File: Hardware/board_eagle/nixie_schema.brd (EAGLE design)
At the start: 150 x 170 mm, 230 parts, among them P1 100k, P2 10k, Q1 BC856B, Q3 BC856B, Q4 BCX70H, Q5 NTF5P03, U2 MC7940N, U3 1V5

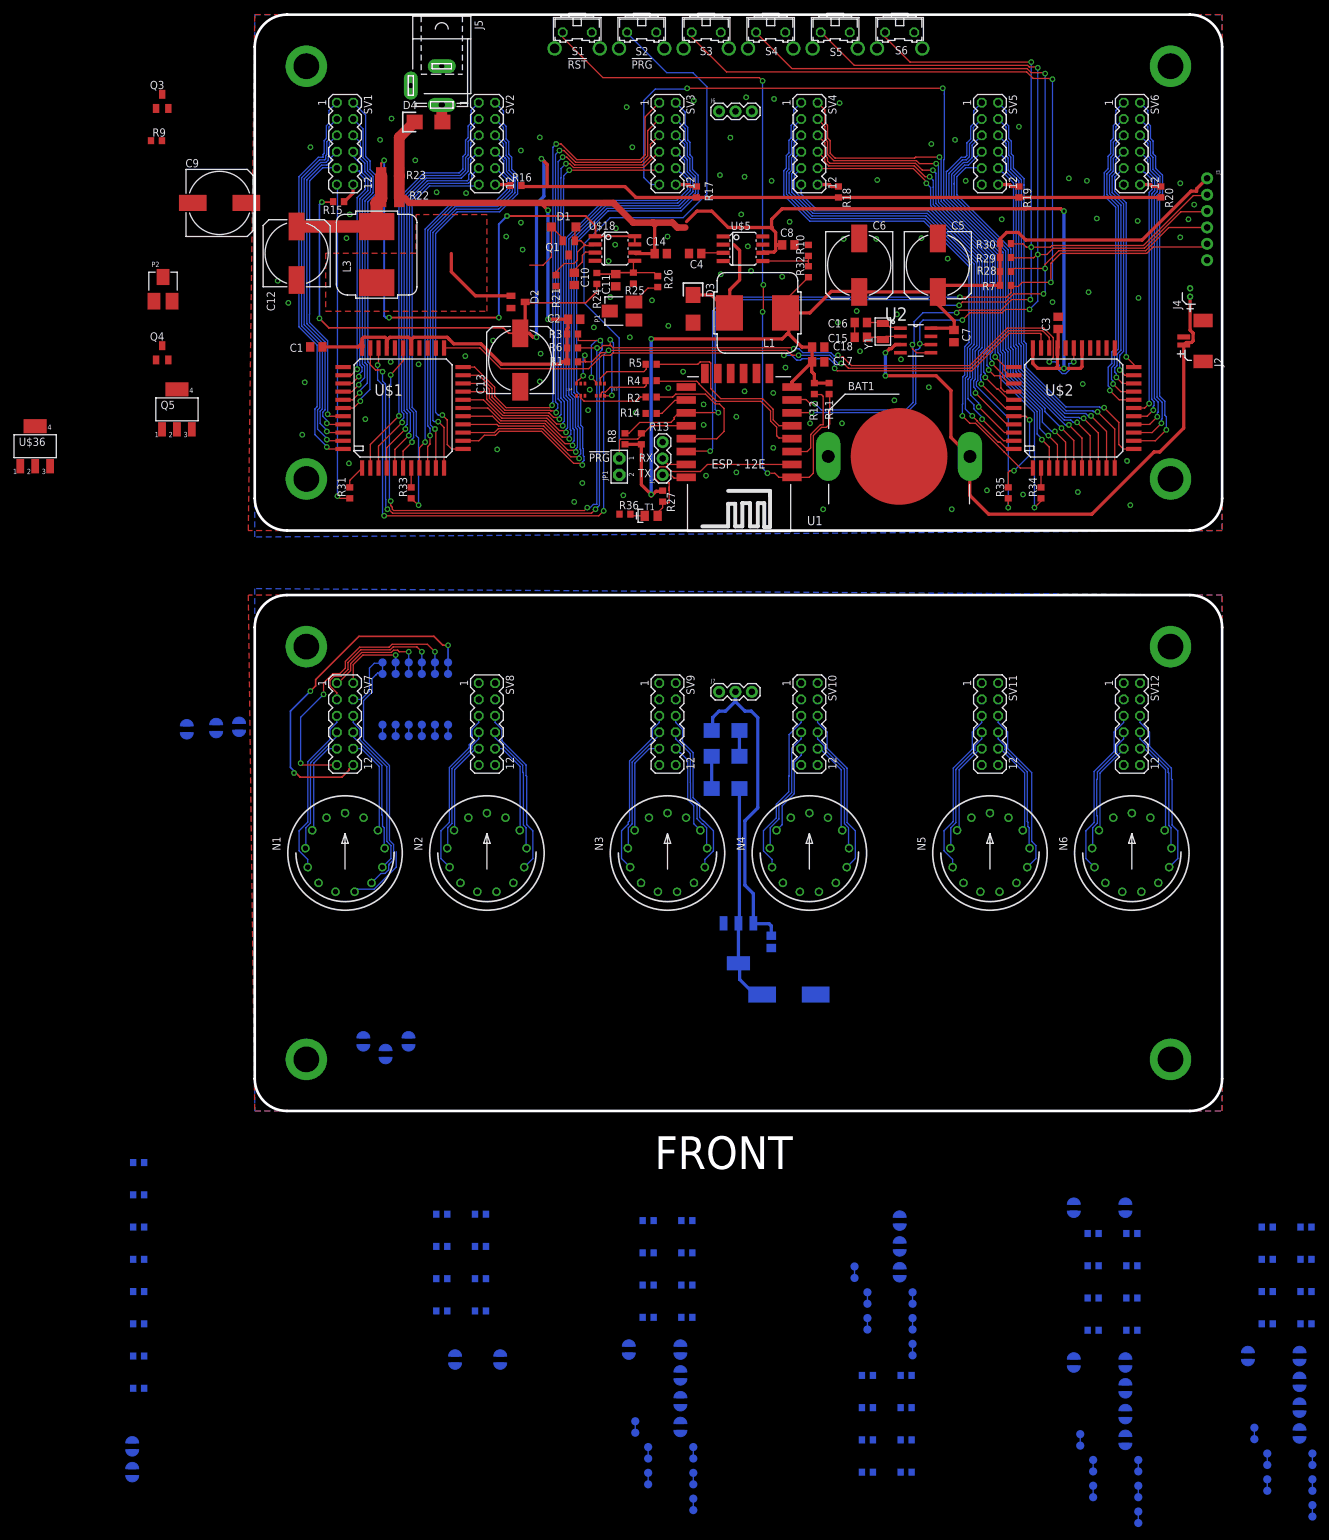
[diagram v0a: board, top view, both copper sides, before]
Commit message: Some more routing of the top board
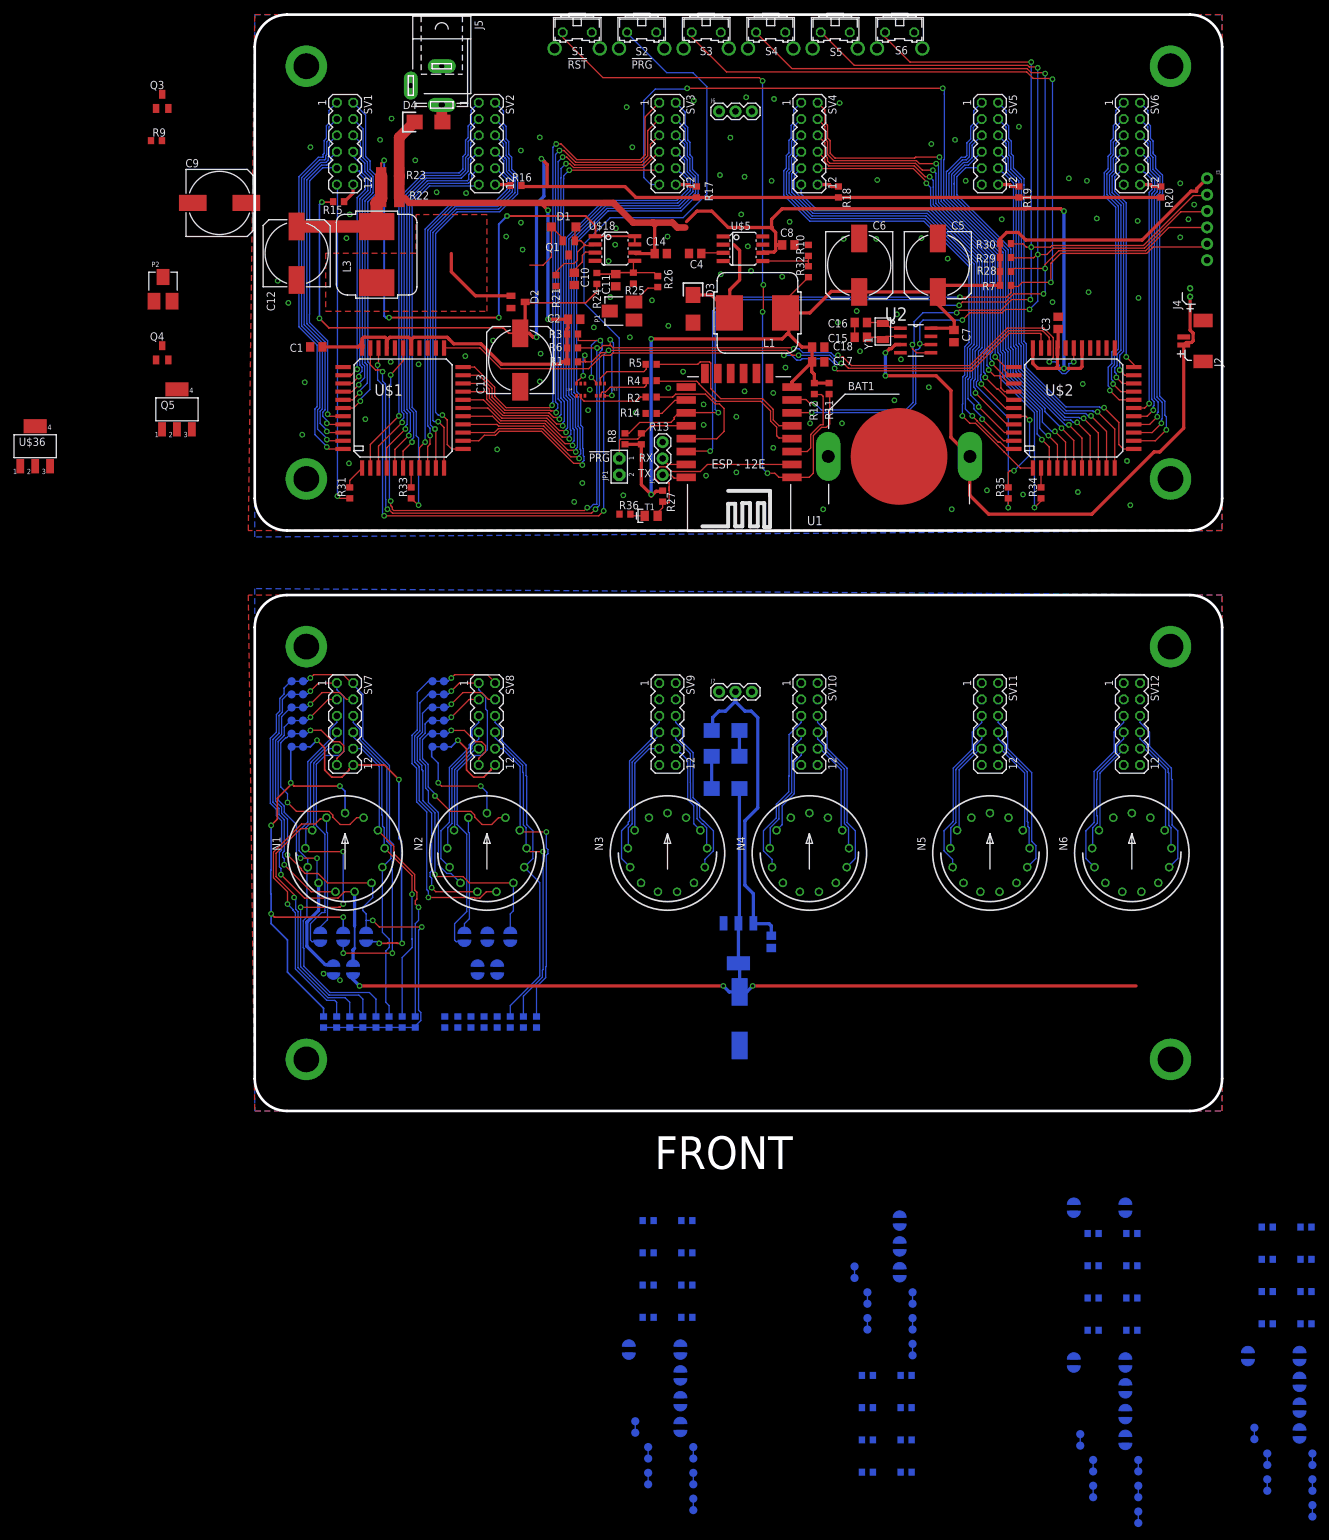
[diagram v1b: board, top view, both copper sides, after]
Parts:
- CUT1, CUT10, CUT11, CUT12, CUT13, CUT14, CUT15, CUT16, CUT17, CUT18, CUT19, CUT2, CUT20, CUT21, CUT22, CUT23, CUT24, CUT25, CUT26, CUT27, CUT28, CUT29, CUT3, CUT30, CUT31, CUT32, CUT33, CUT34, CUT35, CUT36, CUT4, CUT5, CUT6, CUT7, CUT8, CUT9: device nixe_cmp:CUT_TRACE -> nixe_cmp:CUT_TRACE_2
- moved BR2 85.1 mm to (15.2, -68.1), turned to 180 degrees
- moved BR7 80.2 mm to (12.2, -68.1)
- moved R44 65.6 mm to (14.7, -76.2), turned to 270 degrees
- moved R43 62.4 mm to (16.8, -76.2), turned to 270 degrees
- moved BR4 60.8 mm to (37.6, -68.1), turned to 180 degrees
- moved BR3 60.6 mm to (34.5, -68.1)
- moved R42 59.5 mm to (18.8, -76.2), turned to 270 degrees
- moved R41 57.1 mm to (20.8, -76.2), turned to 270 degrees
- moved R40 55.0 mm to (22.9, -76.2), turned to 270 degrees
- moved R39 53.4 mm to (24.9, -76.2), turned to 270 degrees
- moved R52 45.0 mm to (33.5, -76.2), turned to 270 degrees
- moved R51 44.8 mm to (35.6, -76.2), turned to 270 degrees
- moved BR1 42.5 mm to (17.3, -63.0)
- moved R38 40.8 mm to (12.7, -76.2), turned to 270 degrees
- moved R50 40.7 mm to (37.6, -76.2), turned to 270 degrees
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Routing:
- net 1V5: track 34.8 -> 155.6 mm, vias 0 -> 3
- net 1_A_A: track 0.00 -> 72.5 mm, vias 0 -> 5
- net 1_LDP_G: track 0.00 -> 58.9 mm, vias 0 -> 1
- net N$23: track 0.00 -> 52.2 mm, vias 0 -> 1
- net N$10: track 11.3 -> 62.6 mm, vias 1 -> 3
- net 1_7_GRID: track 38.0 -> 87.6 mm, vias 0 -> 3
- net 2_7_GRID: track 0.00 -> 48.8 mm, vias 0 -> 1
- net 2_6_CAT: track 0.00 -> 47.1 mm, vias 0 -> 1
- net 1_6_CAT: track 10.4 -> 57.0 mm, vias 0 -> 1
- net 1_4_CAT: track 0.00 -> 45.9 mm, vias 0 -> 2
- net 1_2_E: track 20.0 -> 64.7 mm, vias 0 -> 3
- net 2_5_NC: track 0.00 -> 40.0 mm, vias 0 -> 1
- net 1_1_F: track 15.0 -> 53.9 mm, vias 0 -> 1
- net 1_5_NC: track 0.00 -> 38.5 mm, vias 0 -> 1
- net N$29: track 15.8 -> 52.6 mm
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
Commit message: Top board routing
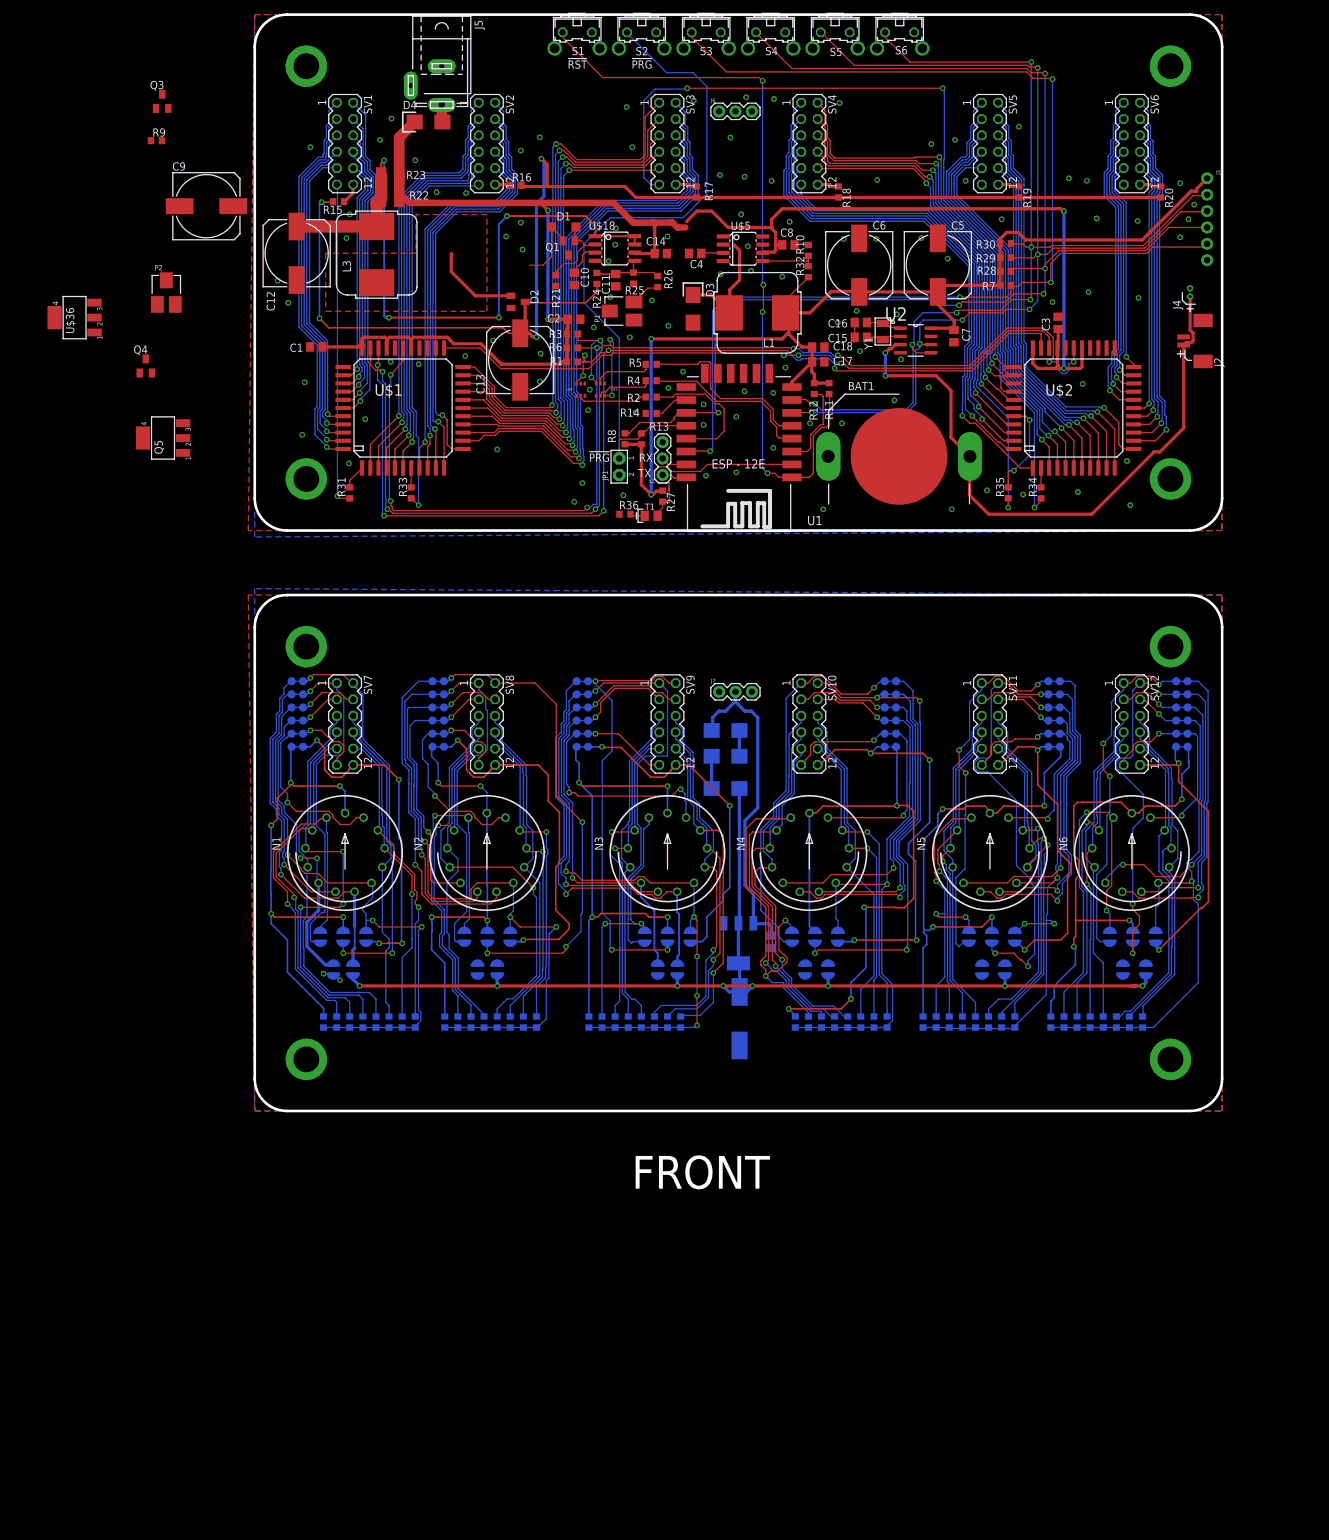
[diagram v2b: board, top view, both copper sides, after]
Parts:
- moved CUT30 130.3 mm to (124.0, -23.4), turned to 270 degrees
- moved CUT36 130.2 mm to (143.8, -23.4), turned to 270 degrees
- moved CUT18 126.8 mm to (50.8, -25.4), turned to 90 degrees
- moved CUT29 121.7 mm to (124.0, -27.4), turned to 270 degrees
- moved CUT35 121.3 mm to (143.8, -27.4), turned to 270 degrees
- moved CUT15 120.1 mm to (50.8, -23.4), turned to 270 degrees
- moved CUT27 119.8 mm to (124.0, -25.4), turned to 90 degrees
- moved CUT33 119.3 mm to (143.8, -25.4), turned to 90 degrees
- moved CUT34 118.2 mm to (143.8, -31.5), turned to 270 degrees
- moved CUT28 118.2 mm to (124.0, -31.5), turned to 270 degrees
- moved CUT17 118.0 mm to (50.8, -29.5), turned to 90 degrees
- moved CUT14 116.8 mm to (50.8, -27.4), turned to 270 degrees
- moved CUT16 116.8 mm to (50.8, -31.5), turned to 90 degrees
- moved CUT32 116.3 mm to (143.8, -29.5), turned to 90 degrees
- moved CUT26 116.3 mm to (124.0, -29.5), turned to 90 degrees
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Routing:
- net 4_A_A: track 0.00 -> 94.0 mm, vias 0 -> 4
- net 3_7_GRID: track 0.00 -> 89.9 mm, vias 0 -> 5
- net 6_7_GRID: track 0.00 -> 84.5 mm, vias 0 -> 1
- net 5_7_GRID: track 0.00 -> 83.1 mm, vias 0 -> 3
- net 4_7_GRID: track 0.00 -> 81.9 mm, vias 0 -> 1
- net 3_A_A: track 0.00 -> 75.6 mm, vias 0 -> 4
- net N$35: track 0.00 -> 75.1 mm, vias 0 -> 4
- net 5_A_A: track 0.00 -> 74.9 mm, vias 0 -> 4
- net 6_A_A: track 0.00 -> 73.1 mm, vias 0 -> 3
- net N$27: track 0.00 -> 68.1 mm, vias 0 -> 3
- net N$41: track 0.00 -> 67.6 mm, vias 0 -> 3
- net N$6: track 8.82 -> 74.7 mm, vias 1 -> 4
- net 3_6_CAT: track 0.00 -> 65.8 mm, vias 0 -> 1
- net N$34: track 0.00 -> 63.6 mm, vias 0 -> 4
- net N$38: track 0.00 -> 60.7 mm, vias 0 -> 1
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
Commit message: More Tob Board Routing
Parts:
- moved C9 2.09 mm to (-9.53, 49.8)
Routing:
- net 4_4_CAT: track 46.3 -> 60.4 mm
- net 5_4_CAT: track 43.1 -> 57.2 mm
- net 2_4_CAT: track 33.8 -> 47.6 mm
- net 6_4_CAT: track 43.1 -> 56.9 mm
- net 5_6_CAT: track 43.6 -> 55.2 mm
- net 6_6_CAT: track 42.0 -> 53.5 mm
- net 2_6_CAT: track 51.0 -> 62.5 mm
- net 4_6_CAT: track 47.1 -> 58.3 mm
- net 2_LDP_G: track 57.0 -> 59.3 mm
- net N$23: track 52.2 -> 53.2 mm
